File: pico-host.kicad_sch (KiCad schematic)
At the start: 52 parts, among them J1 USB_C_Receptacle_USB2.0, J2 I2C, J4 Conn, J5 Conn, J6 BAT, Q1 BSS83P, SW1 SW_Push, SW2 SW_Push, U1 RP2040, U2 W25Q128JVS, U3 AP2112K-3.3, U4 MCP73831, Y1 24MHz

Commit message: Tracks almost finished
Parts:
- Q1: footprint Package_DFN_QFN:Diodes_DFN1006-3 -> DMG3415UFY4Q-7:TRANS_DMG3415UFY4Q-7
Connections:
- net VHI: now reaches C3.1, D1.1 (K), Q1.2 (S), R9.1, U3.1 (VIN)
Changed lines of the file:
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@@
 	(wire
 		(pts
+			(xy 41.91 38.1) (xy 41.91 39.37)
+		)
+		(stroke
+			(width 0)
+			(type default)
+		)
+	)
+	(wire
+		(pts
 			(xy 110.49 172.72) (xy 97.79 172.72)
 		)
@@
 		(on_board yes)
 		(dnp no)
-		(fields_autoplaced yes)
 		(property "Reference" "Q1"
-			(at 35.56 29.2099 0)
+			(at 34.544 26.162 0)
 			(effects
 				(font
@@
 		)
 		(property "Value" "BSS83P"
-			(at 35.56 31.7499 0)
+			(at 34.544 28.702 0)
 			(effects
 				(font
@@
 			)
 		)
-		(property "Footprint" "Package_DFN_QFN:Diodes_DFN1006-3"
+		(property "Footprint" "DMG3415UFY4Q-7:TRANS_DMG3415UFY4Q-7"
 			(at 34.29 32.385 0)
 			(effects
@@
 					(unit 1)
 				)
+			)
+		)
+	)
+	(symbol
+		(lib_id "power:VBUS")
+		(at 41.91 38.1 0)
+		(unit 1)
+		(exclude_from_sim no)
+		(in_bom yes)
+		(on_board yes)
+		(dnp no)
+		(fields_autoplaced yes)
+		(property "Reference" "#PWR076"
+			(at 41.91 41.91 0)
+			(effects
+				(font
+					(size 1.27 1.27)
+				)
+				(hide yes)
+			)
+		)
+		(property "Value" "VHI"
+			(at 41.91 33.02 0)
+			(effects
+				(font
+					(size 1.27 1.27)
+				)
+			)
+		)
+		(property "Footprint" ""
+			(at 41.91 38.1 0)
+			(effects
+				(font
+					(size 1.27 1.27)
+				)
+				(hide yes)
+			)
+		)
+		(property "Datasheet" ""
+			(at 41.91 38.1 0)
+			(effects
+				(font
+					(size 1.27 1.27)
+				)
+				(hide yes)
+			)
+		)
+		(property "Description" "Power symbol creates a global label with name \"VBUS\""
+			(at 41.91 38.1 0)
+			(effects
+				(font
+					(size 1.27 1.27)
+				)
+				(hide yes)
+			)
+		)
+		(pin "1"
+		)
+		(instances
+			(project "pico-host"
+				(path "/1a6f4a6d-c05c-4dd5-b6d1-65b1c9a9285b"
+					(reference "#PWR076")
+					(unit 1)
+				)

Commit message: Finished Tracks
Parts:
- removed C6: 1uF, Capacitor_SMD:C_0603_1608Metric, symbol Device:C_Small
- C9: footprint Capacitor_SMD:C_0603_1608Metric -> Capacitor_SMD:C_0402_1005Metric
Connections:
- net +3V3: no longer D5.1 (VDD)
- net GPIO14: now also J4.11 (Pin_11)
- net GPIO15: now also J4.12 (Pin_12)
- net GPIO18: no longer J4.11 (Pin_11)
- net GPIO19: no longer J4.12 (Pin_12)
- net GPIO20: now also D5.1 (VDD); no longer D5.4 (DIN), J4.13 (Pin_13)
- net GPIO21: now also D5.4 (DIN)
- net GPIO8: now also J4.13 (Pin_13)

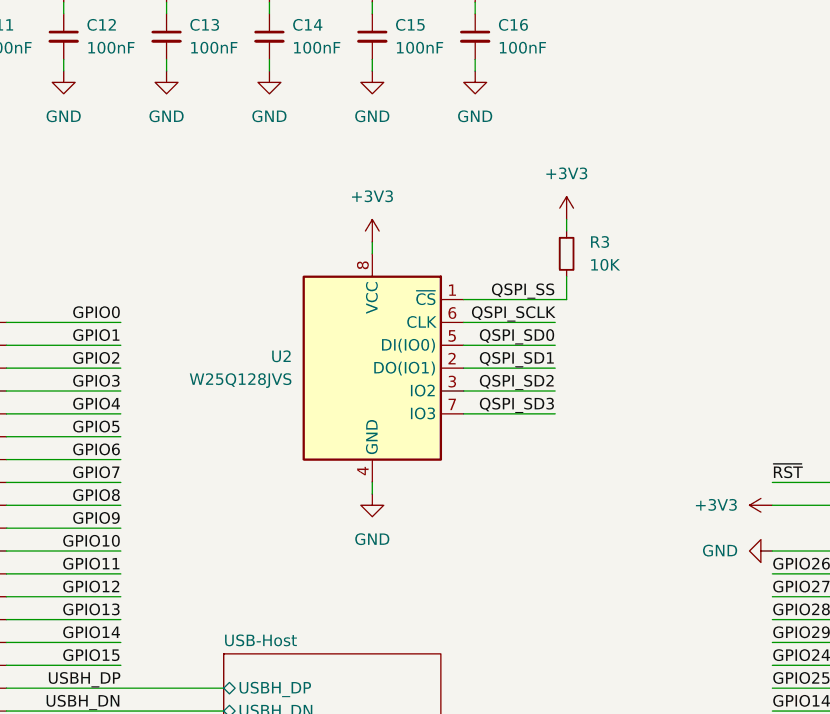
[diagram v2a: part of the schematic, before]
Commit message: Added qr logo, doc/images, updated README
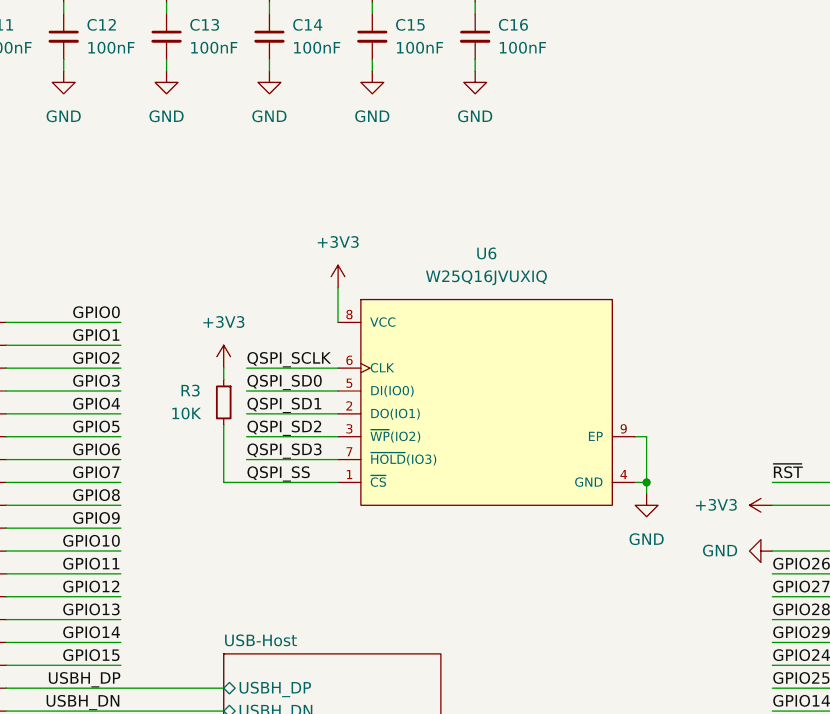
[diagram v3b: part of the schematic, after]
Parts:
- removed U2: W25Q128JVS, SPI-Flash:USON-8-3x4, symbol Memory_Flash:W25Q128JVS
- added U6: W25Q16JVUXIQ, W25Q16JVUXIQ:Winbond-UX-0-0-IPC_B, symbol W25Q16JVUXIQ:W25Q16JVUXIQ
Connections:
- net +3V3: now also U6.8 (VCC)
- net GND: now also U6.4 (GND), U6.9 (EP)
- net QSPI_SCLK: now also U6.6 (CLK)
- net QSPI_SD0: now also U6.5 (DI(IO0))
- net QSPI_SD1: now also U6.2 (DO(IO1))
- net QSPI_SD2: now also U6.3 (~{WP}(IO2))
- net QSPI_SD3: now also U6.7 (~{HOLD}(IO3))
- net QSPI_SS: now also U6.1 (~{CS})
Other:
- moved on the sheet: R3
